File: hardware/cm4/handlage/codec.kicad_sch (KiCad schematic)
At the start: 15 parts, among them U2 TLV320AIC3204IRHBR, U4 AP2112K-3.3, U6 12MHz

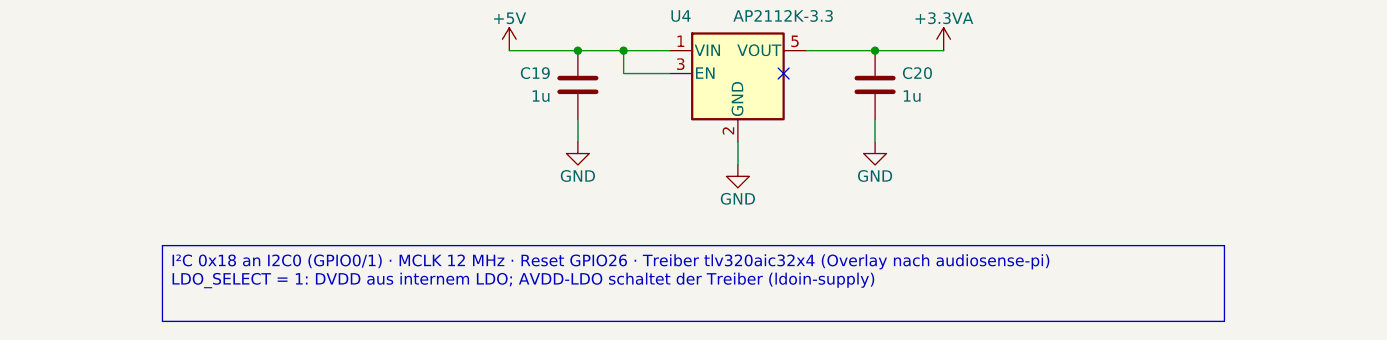
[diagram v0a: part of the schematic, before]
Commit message: CM4-Schaltplan: Handänderungen übernommen (Handlage für 8 Blätter, 2 Texte zurückgeführt); Kastenhöhen aus gemessenen Zeichenbreiten
Co-Authored-By: Claude Opus 5.5 <noreply@anthropic.com>
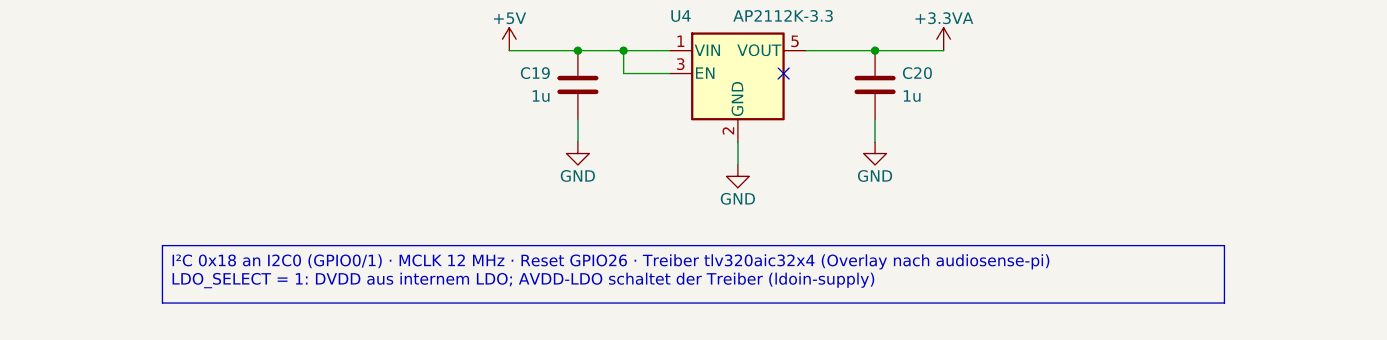
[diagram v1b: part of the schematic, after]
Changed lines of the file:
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@@
 	)
 (text "Analogversorgung 3,3 V" (exclude_from_sim no) (at 199.9 177.29 0) (effects (font (size 1.524 1.524) italic) (justify left bottom)))
-	(text_box "I²C 0x18 an I2C0 (GPIO0/1) · MCLK 12 MHz · Reset GPIO26 · Treiber tlv320aic32x4 (Overlay nach audiosense-pi)\nLDO_SELECT = 1: DVDD aus internem LDO; AVDD-LDO schaltet der Treiber (ldoin-supply)" (exclude_from_sim no) (at 148.15 210.89 0) (size 118 8.42) (margins 0.9525 0.9525 0.9525 0.9525) (stroke (width 0.1) (type solid) (color 132 132 132 1)) (fill (type color) (color 255 255 230 1)) (effects (font (size 1.27 1.27)) (justify left top)))
+	(text_box "I²C 0x18 an I2C0 (GPIO0/1) · MCLK 12 MHz · Reset GPIO26 · Treiber tlv320aic32x4 (Overlay nach audiosense-pi)\nLDO_SELECT = 1: DVDD aus internem LDO; AVDD-LDO schaltet der Treiber (ldoin-supply)" (exclude_from_sim no) (at 148.15 210.89 0) (size 118 6.38) (margins 0.9525 0.9525 0.9525 0.9525) (stroke (width 0.1) (type solid) (color 132 132 132 1)) (fill (type color) (color 255 255 230 1)) (effects (font (size 1.27 1.27)) (justify left top)))
 	)
